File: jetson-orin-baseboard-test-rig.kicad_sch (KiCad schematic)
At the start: 64 parts, among them J1 PinHeader_2x6_P2.54mm_Drill1.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, J10 Harwin_1x1_H17.75mm_Drill0.8m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, J11 Harwin_1x1_H17.75mm_Drill0.8m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, J12 Harwin_1x1_H17.75mm_Drill0.8m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, J13 Harwin_1x1_H17.75mm_Drill0.8m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, J14 Harwin_1x1_H17.75mm_Drill0.8m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, J15 Harwin_1x1_H17.75mm_Drill0.8m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, J16 Harwin_1x1_H17.75mm_Drill0.8m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, J17 Harwin_1x1_H17.75mm_Drill0.8m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, J18 Harwin_1x1_H17.75mm_Drill0.8m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, J19 Harwin_1x1_H17.75mm_Drill0.8m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, J2 PinHeader_2x6_P2.54mm_Drill1.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, J20 Harwin_1x1_H17.75mm_Drill0.8m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, J21 Harwin_1x1_H17.75mm_Drill0.8m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, J22 Harwin_1x1_H17.75mm_Drill0.8m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, J23 Harwin_1x1_H17.75mm_Drill0.8m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, J24 Harwin_1x1_H17.75mm_Drill0.8m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, J25 Harwin_1x1_H17.75mm_Drill0.8m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, J26 Harwin_1x1_H17.75mm_Drill0.8m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, J27 Harwin_1x1_H17.75mm_Drill0.8m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, J28 Harwin_1x1_H17.75mm_Drill0.8m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, J29 Harwin_1x1_H17.75mm_Drill0.8m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, J3 PinHeader_2x6_P2.54mm_Drill1.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, J30 Harwin_1x1_H17.75mm_Drill0.8m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, J4 PinHeader_2x6_P2.54mm_Drill1.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, J5 PinHeader_2x6_P2.54mm_Drill1.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, J6 PinHeader_2x6_P2.54mm_Drill1.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, J7 PinHeader_2x6_P2.54mm_Drill1.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, J8 Harwin_1x1_H17.75mm_Drill0.8m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, J9 Harwin_1x1_H17.75mm_Drill0.8m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, Q1 BSS84

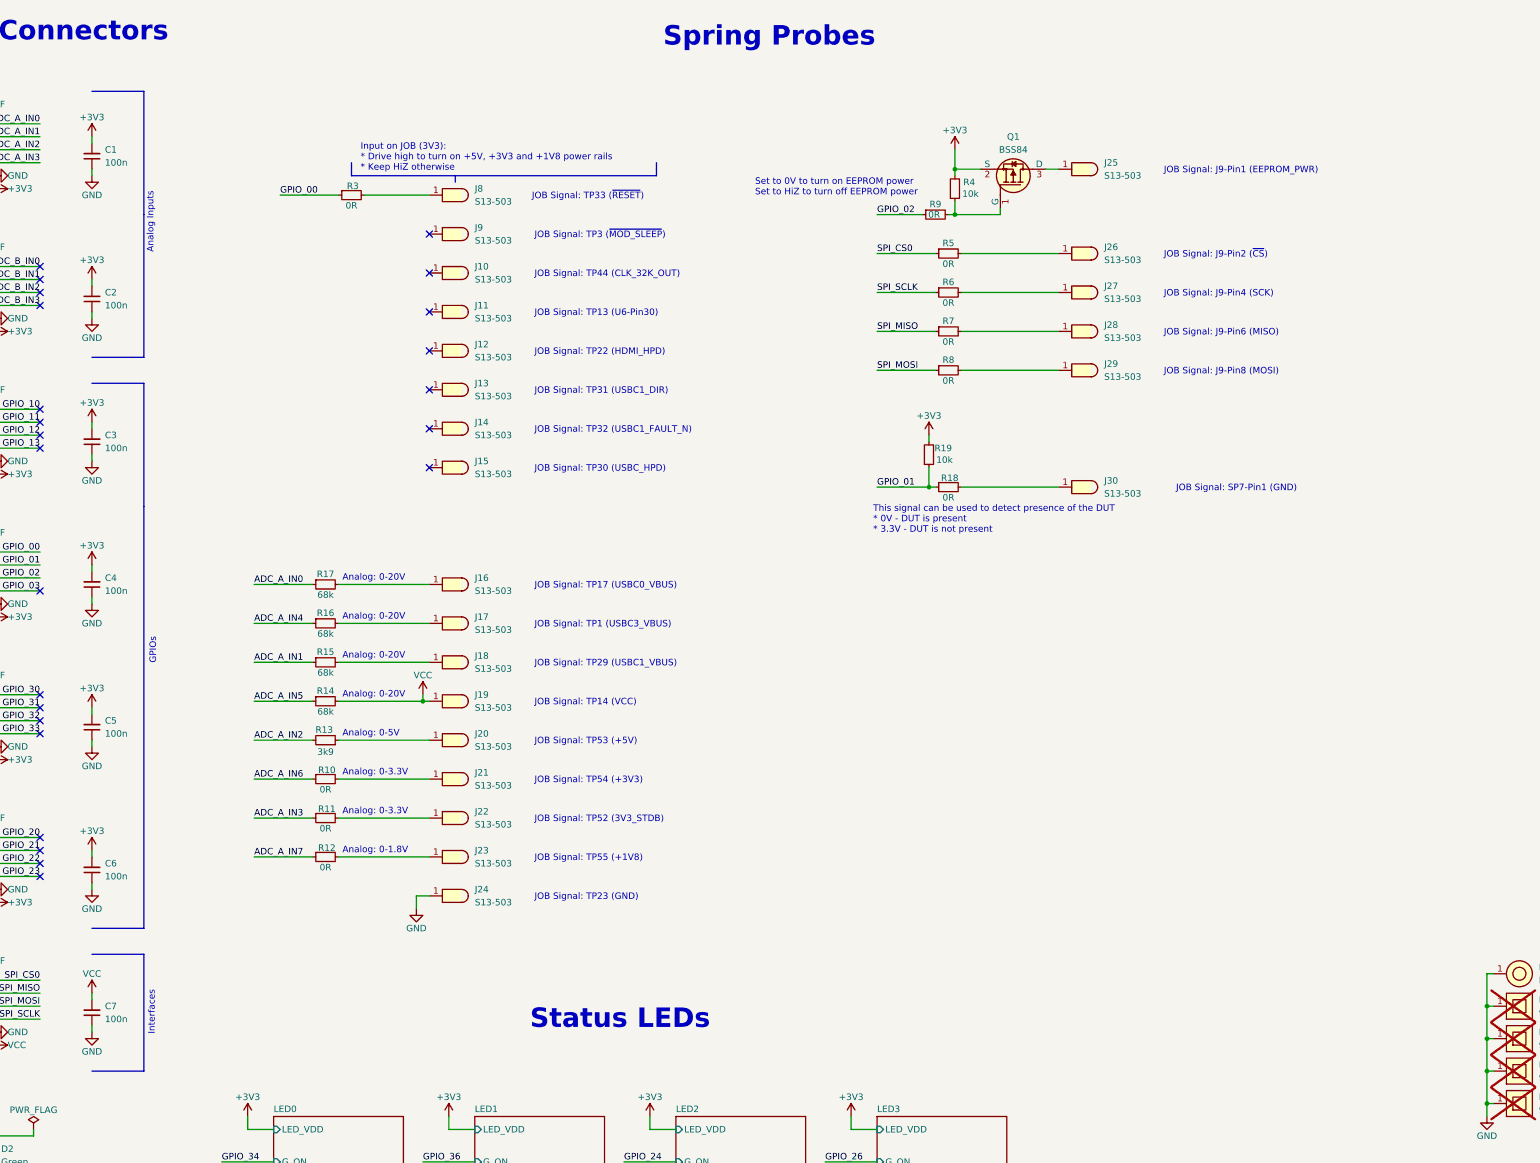
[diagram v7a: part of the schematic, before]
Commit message: [#77400] Add TVS
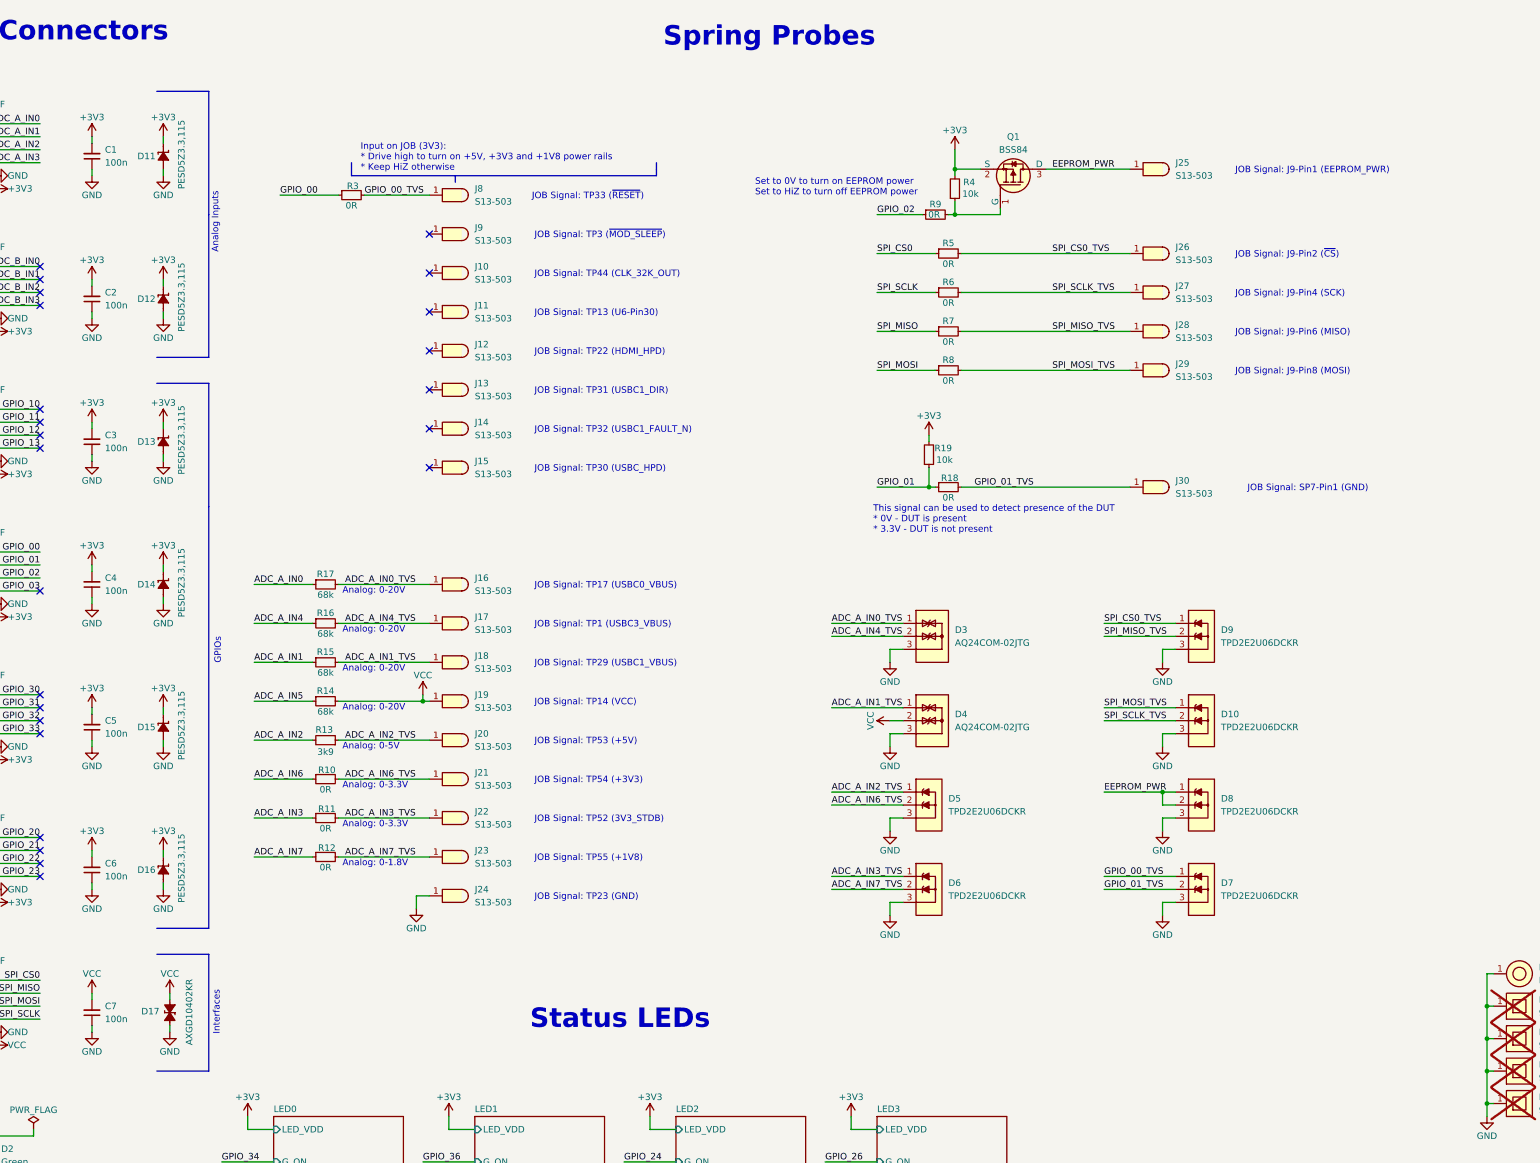
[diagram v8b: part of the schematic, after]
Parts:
- added D10, D5, D6, D7, D8, D9: TPD2E2U06_SC70, antmicro-footprints:SC70-3, symbol antmicroTVSDiodes:TPD2E2U06_SC70
- added D11, D12, D13, D14, D15, D16: PESD5Z3.3, antmicro-footprints:SOD-523, symbol antmicroTVSDiodes:PESD5Z3.3
- added D17: AXGD10402KR, antmicro-footprints:D_0402_1005Metric, symbol antmicroTVSDiodes:AXGD10402KR
- added D3, D4: AQ24COM-02, antmicro-footprints:SC70-3, symbol antmicroTVSDiodes:AQ24COM-02
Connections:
- net +3V3: now also D11.1 (C), D12.1 (C), D13.1 (C), D14.1 (C), D15.1 (C), D16.1 (C)
- net GND: now also D10.3, D11.2 (A), D12.2 (A), D13.2 (A), D14.2 (A), D15.2 (A), D16.2 (A), D17.1 (C), D3.3, D4.3, D5.3, D6.3, D7.3, D8.3, D9.3
- net VCC: now also D17.2 (A), D4.2
- net SPI_SCLK_TVS: now reaches J27.1, R6.2
- net SPI_SCLK_TVS: now also D10.2
- net ADC_A_IN7_TVS: now reaches J23.1, R12.2
- net ADC_A_IN7_TVS: now also D6.2
- net ADC_A_IN3_TVS: now reaches J22.1, R11.2
- net ADC_A_IN3_TVS: now also D6.1
- net ADC_A_IN6_TVS: now reaches J21.1, R10.2
- net ADC_A_IN6_TVS: now also D5.2
- net ADC_A_IN1_TVS: now reaches J18.1, R15.2
- net ADC_A_IN1_TVS: now also D4.1
- net SPI_MISO_TVS: now reaches J28.1, R7.2
- net SPI_MISO_TVS: now also D9.2
- net ADC_A_IN0_TVS: now reaches J16.1, R17.2
- net ADC_A_IN0_TVS: now also D3.1
- net ADC_A_IN2_TVS: now reaches J20.1, R13.1
- net ADC_A_IN2_TVS: now also D5.1
- net GPIO_00_TVS: now reaches J8.1, R3.2
- net GPIO_00_TVS: now also D7.1
- net EEPROM_PWR: now reaches J25.1, Q1.3 (D)
- net EEPROM_PWR: now also D8.1, D8.2
- net SPI_CS0_TVS: now reaches J26.1, R5.2
- net SPI_CS0_TVS: now also D9.1
- net SPI_MOSI_TVS: now reaches J29.1, R8.2
- net SPI_MOSI_TVS: now also D10.1
- net ADC_A_IN4_TVS: now reaches J17.1, R16.2
- net ADC_A_IN4_TVS: now also D3.2
- net GPIO_01_TVS: now reaches J30.1, R18.2
- net GPIO_01_TVS: now also D7.2
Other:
- moved on the sheet: J25, J26, J27, J28, J29, J30
